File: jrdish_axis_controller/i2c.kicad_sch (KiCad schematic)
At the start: 18 parts, among them CN7 SM04B-SRSS-TB (LF)(SN), CN8 SM04B-SRSS-TB (LF)(SN), U5 LTC4311ISC6#TRPBF, U6 LM75BIMX-5/NOPB, U7 W25Q32JVSSIQ_C179173

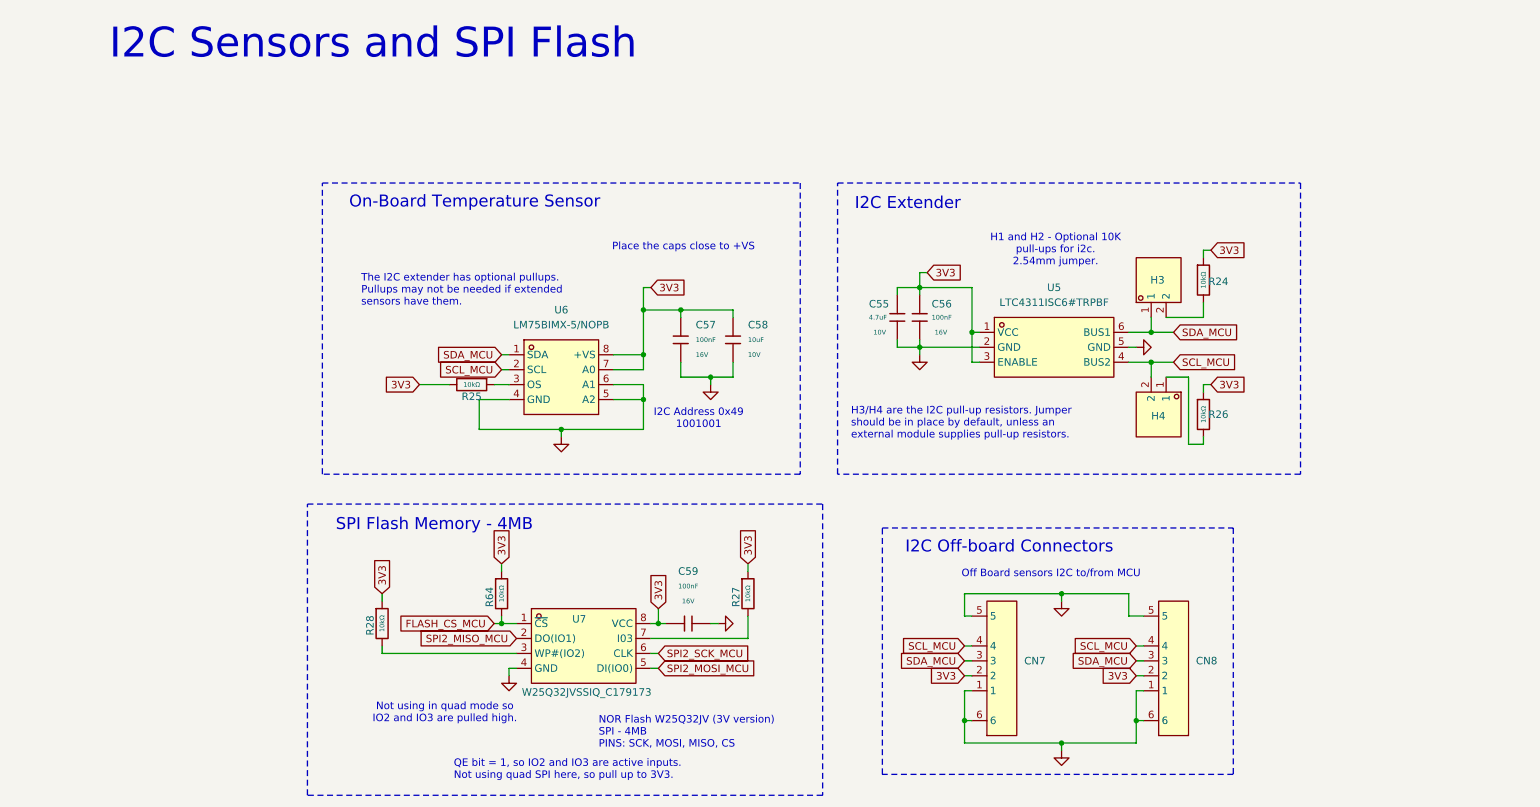
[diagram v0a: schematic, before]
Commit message: Limit switches with mosfets
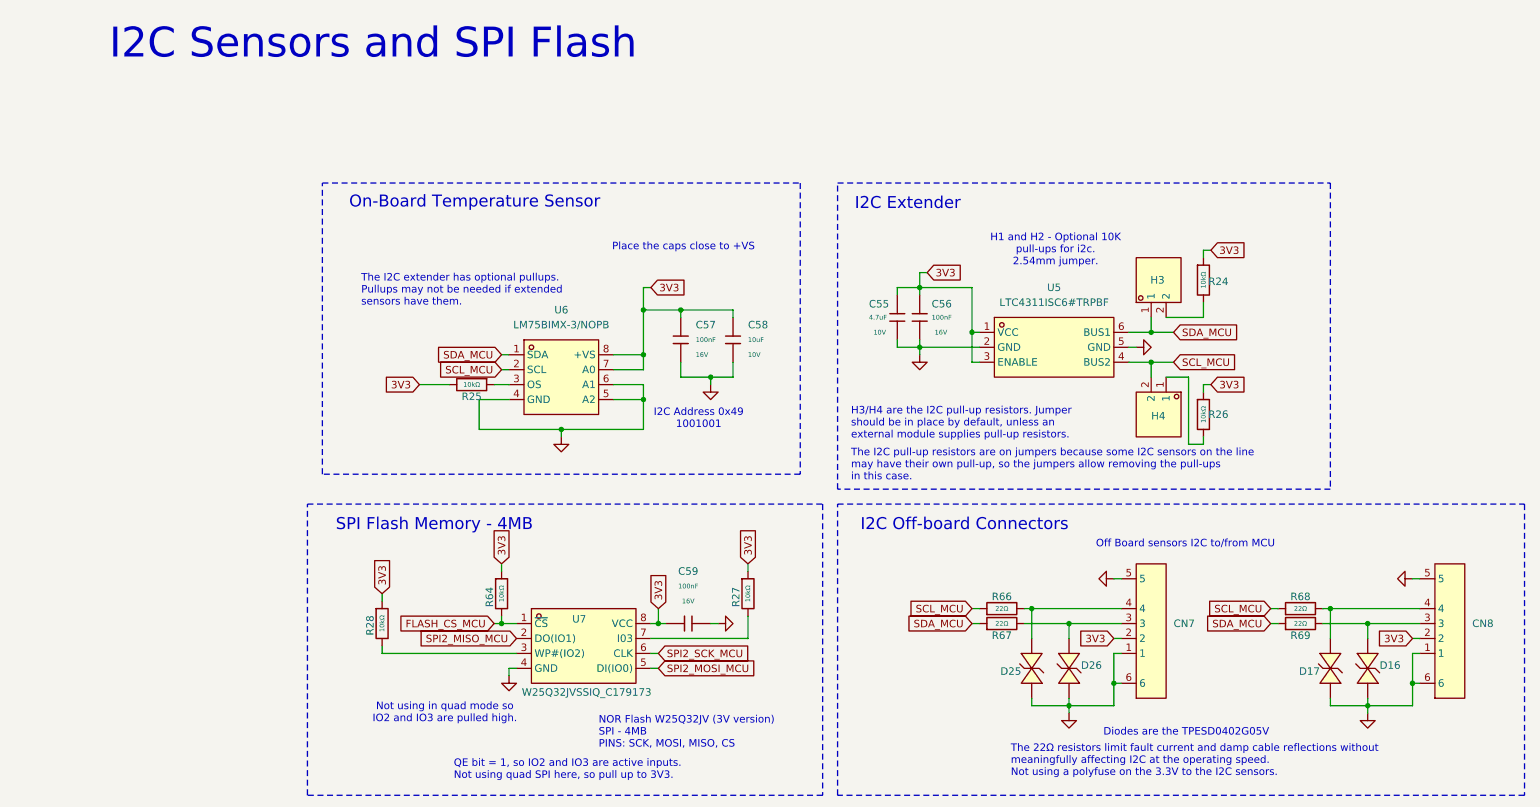
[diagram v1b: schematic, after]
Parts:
- removed U6: LM75BIMX-5/NOPB, MyParts:SOIC-8_L4.9-W3.9-P1.27-LS6.0-BL, symbol MyParts:LM75BIMX-5_NOPB
- added D16, D17, D25, D26: TPESD0402G05V, MyParts:D0402-BI, symbol MyParts:TPESD0402G05V
- added R66, R67, R68, R69: 22Ω, PCM_JLCPCB:R_0402, symbol PCM_JLCPCB-Resistors:0402,22Ω
- added U6: LM75BIMX-3/NOPB, MyParts:SOIC-8_L4.9-W3.9-P1.27-LS6.0-BL, symbol MyParts:LM75BIMX-3_NOPB
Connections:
- net 3V3: now also U6.7 (A0), U6.8 (+VS)
- net SCL_MCU: now also R66.1, R68.1, U6.2 (SCL); no longer CN7.4, CN8.4
- net SDA_MCU: now also R67.1, R69.1, U6.1 (SDA); no longer CN7.3, CN8.3
- net at R25.1: now also U6.3 (OS)
- net GND: now reaches C55.2, C56.2, U5.2 (GND)
- net GND: now also C57.2, C58.2, C59.2, CN7.1, CN7.5, CN7.6, CN8.1, CN8.5, CN8.6, U5.5 (GND), U7.4 (GND), D16.2 (A), D17.2 (A), D25.2 (A), D26.2 (A), U6.4 (GND), U6.5 (A2), U6.6 (A1)
- new net: CN7.3, D26.1 (K), R67.2
- new net: CN7.4, D25.1 (K), R66.2
- new net: CN8.3, D16.1 (K), R69.2
- new net: CN8.4, D17.1 (K), R68.2
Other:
- note added: "Diodes are the TPESD0402G05V"
- note added: "The 22Ω resistors limit fault current and damp cable reflections without meaningfully affecting I2C at the operating speed. Not using a polyfuse on the 3.3V to the I2C sensors."
- note added: "The I2C pull-up resistors are on jumpers because some I2C sensors on the line may have their own pull-up, so the jumpers allow removing the pull-ups in this case."
- moved on the sheet: CN8

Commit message: Refinements...
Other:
- note added: "I2C sensors may include the Adafruit sensors which may have their own pull-up resistors. So H3 and H4 allows you to not have I2C on-board."
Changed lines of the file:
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@@
+		)
+	)
+	(text "I2C sensors may include the Adafruit sensors which\nmay have their own pull-up resistors. So H3 and H4\nallows you to not have I2C on-board."
+		(exclude_from_sim no)
+		(at 189.484 40.132 0)
+		(effects
+			(font
+				(size 1.27 1.27)
+			)
 		)
 	)
